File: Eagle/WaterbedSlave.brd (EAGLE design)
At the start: 55.7 x 50 mm, 4 parts

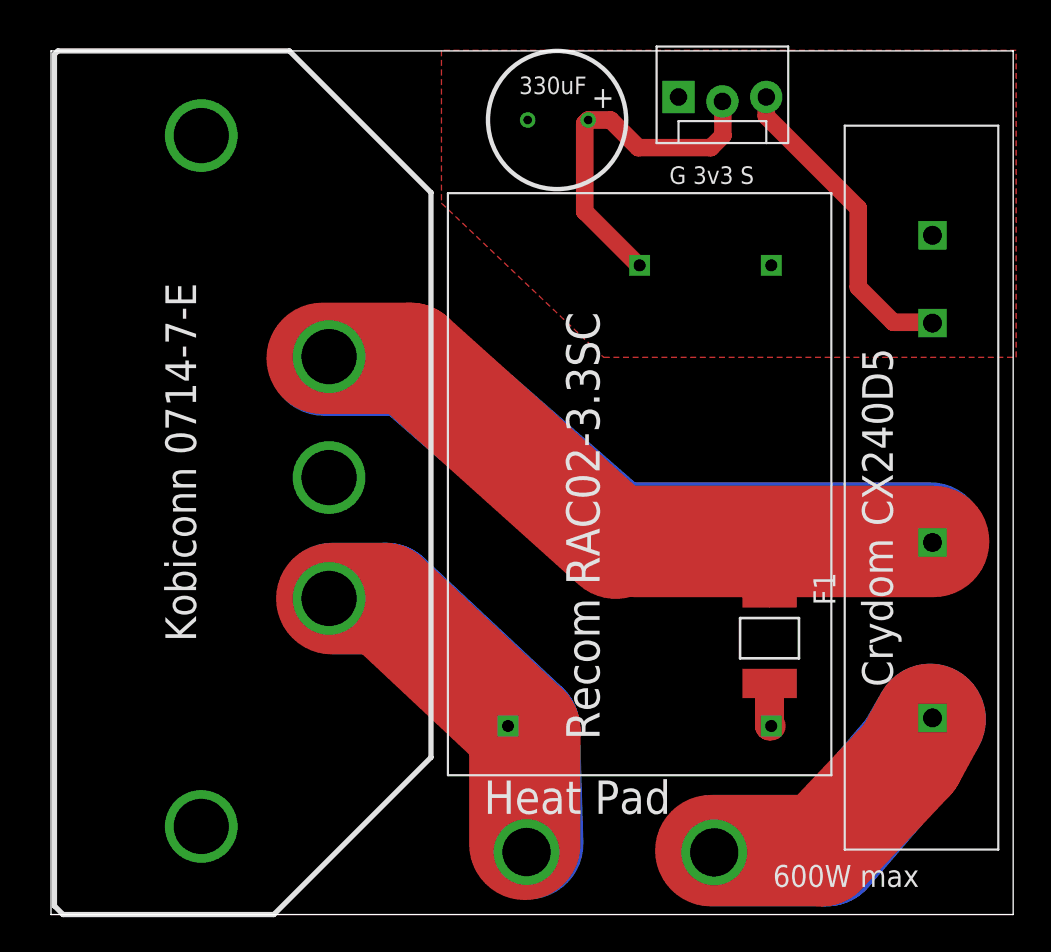
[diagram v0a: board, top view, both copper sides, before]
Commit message: Fixed backwards supply footprint
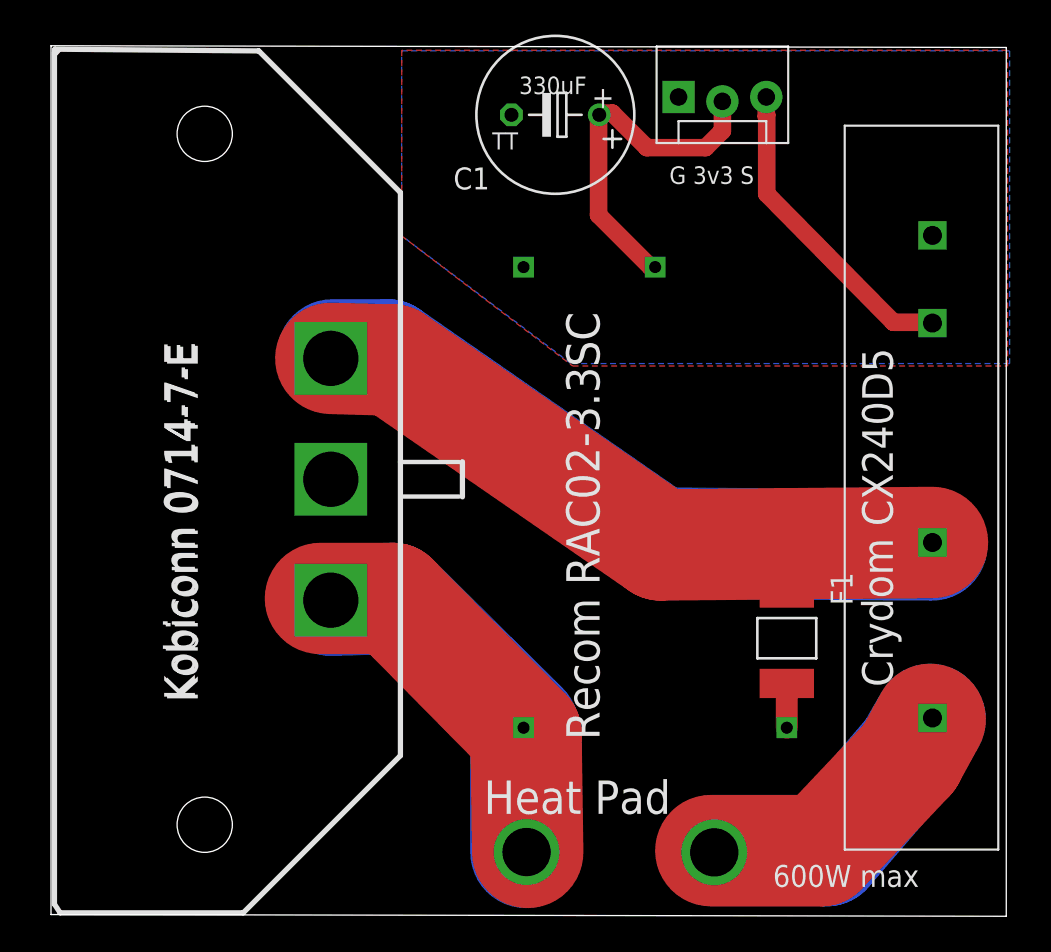
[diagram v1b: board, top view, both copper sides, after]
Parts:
- added C1: (no value), resistor:TT5D9
- added U$3: IEC, CuriousTech:IEC
- moved F1 1.00 mm to (42.6, 16.0)
- moved U$1 0.91 mm to (35.0, 24.8), flipped to the bottom
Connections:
- new net G: U$3.G
- new net N$1: U$1.P$1, U$3.L
- net GND: now also C1.-
- net N$12: now also U$1.P$2; no longer U$1.P$1
- net N$14: now also U$3.H
- net N$15: now also C1.+
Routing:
- net N$7: track 39.0 -> 0.00 mm
- net N$2: track 0.00 -> 38.1 mm, vias 1 -> 0
- net N$14: track 12.4 -> 41.0 mm
- net L: track 20.8 -> 0.00 mm
- net N$8: track 20.8 -> 0.00 mm
- net N$1: track 0.00 -> 14.2 mm, vias 1 -> 0
- net N$3: track 21.1 -> 6.90 mm
- net N$4: track 17.3 -> 22.1 mm
- added copper zone on layer 16, net GND
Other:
- board size 55.7 x 50 mm -> 55.3 x 50.4 mm

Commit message: Update WaterbedSlave.brd
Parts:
- removed U$1: RAC5A240VAC, CuriousTech:RAC3V3
- added JP2, JP3: (no value), SparkFun-Connectors:1X01_2MM
- added SUPP: RAC02-3.3SC, CuriousTech:RAC02-3.3SC
- C1: value (none) -> 330uF
- U$3: value IEC -> IEC 0714-7-E
- moved U$2 2.30 mm to (48.7, 25.3)
- moved U$3 1.00 mm to (7.90, 25.2)
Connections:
- removed net G: U$3.G
- new net N$6: JP2.1, U$2.P$4
- net GND: now also SUPP.3V3; no longer U$1.P$3
- net N$1: now also JP3.1, SUPP.AC1; no longer U$1.P$1
- net N$12: now also SUPP.AC2; no longer U$1.P$2
- net N$15: now also SUPP.GND; no longer U$1.P$4
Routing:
- net N$5: track 16.3 -> 0.00 mm
- net N$11: track 16.3 -> 0.00 mm
- net N$6: track 0.00 -> 15.8 mm
- net N$3: track 6.90 -> 21.7 mm
- net N$1: track 14.2 -> 22.7 mm
- net N$4: track 22.1 -> 15.8 mm
- net N$14: track 41.0 -> 39.7 mm
- net N$2: track 38.1 -> 37.0 mm
- net N$15: track 20.5 -> 21.5 mm
- net N$12: track 2.56 -> 3.56 mm
- net N$16: track 18.5 -> 17.7 mm
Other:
- board size 55.3 x 50.4 mm -> 52.8 x 50.4 mm
- board text removed: "+"
- board text removed: "330uF"
- board text removed: "Crydom CX240D5"
- board text removed: "Kobiconn 0714-7-E"
- board text removed: "Recom RAC02-3.3SC"

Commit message: Updated PPTC
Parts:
- F1: device dp_devices:PTC1812L -> SparkFun-Capacitors:CAP-PTH-5MM
- moved F1 20.7 mm to (22.0, 14.3), turned to 90 degrees
- moved C1 0.40 mm to (29.6, 46.3)
- moved JP3 0.40 mm to (30.1, 3.80)
- moved JP1 0.40 mm to (36.7, 47.2)
- moved JP2 0.40 mm to (38.4, 3.90)
- moved SUPP 0.40 mm to (35.3, 24.2)
- moved U$2 0.40 mm to (49.1, 25.3)
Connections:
- removed net N$12: F1.2, SUPP.AC2
- new net N$5: F1.2, SUPP.AC1
- net N$1: now also F1.1; no longer SUPP.AC1
- net N$14: now also SUPP.AC2; no longer F1.1
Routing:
- net N$1: track 22.7 -> 36.2 mm
- net N$5: track 0.00 -> 8.95 mm
- net N$14: track 39.7 -> 48.7 mm
- net N$3: track 21.7 -> 29.5 mm
- net N$12: track 3.56 -> 0.00 mm
- net N$15: track 21.5 -> 20.2 mm
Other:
- board size 52.8 x 50.4 mm -> 53.2 x 50.4 mm
